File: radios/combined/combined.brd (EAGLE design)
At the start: 31.9 x 30.9 mm, 20 parts

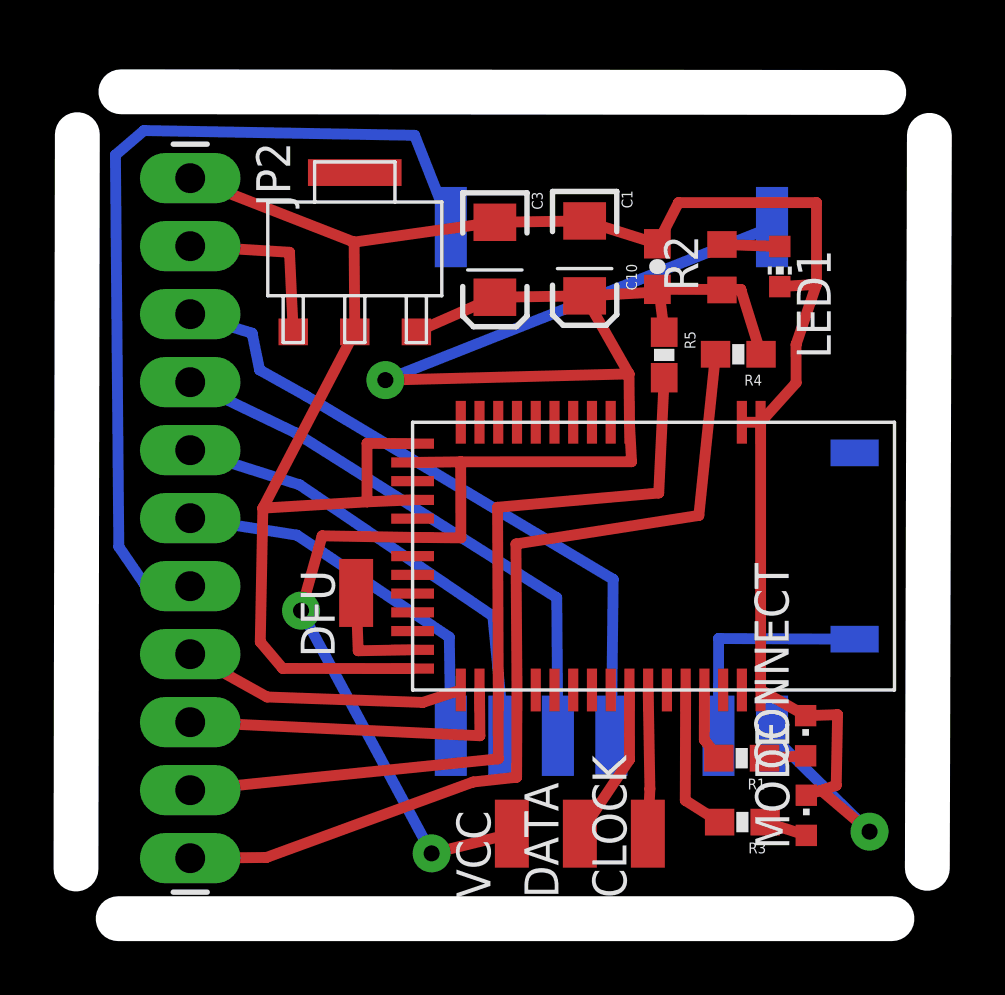
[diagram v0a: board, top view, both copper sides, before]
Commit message: redesigned radios breakout
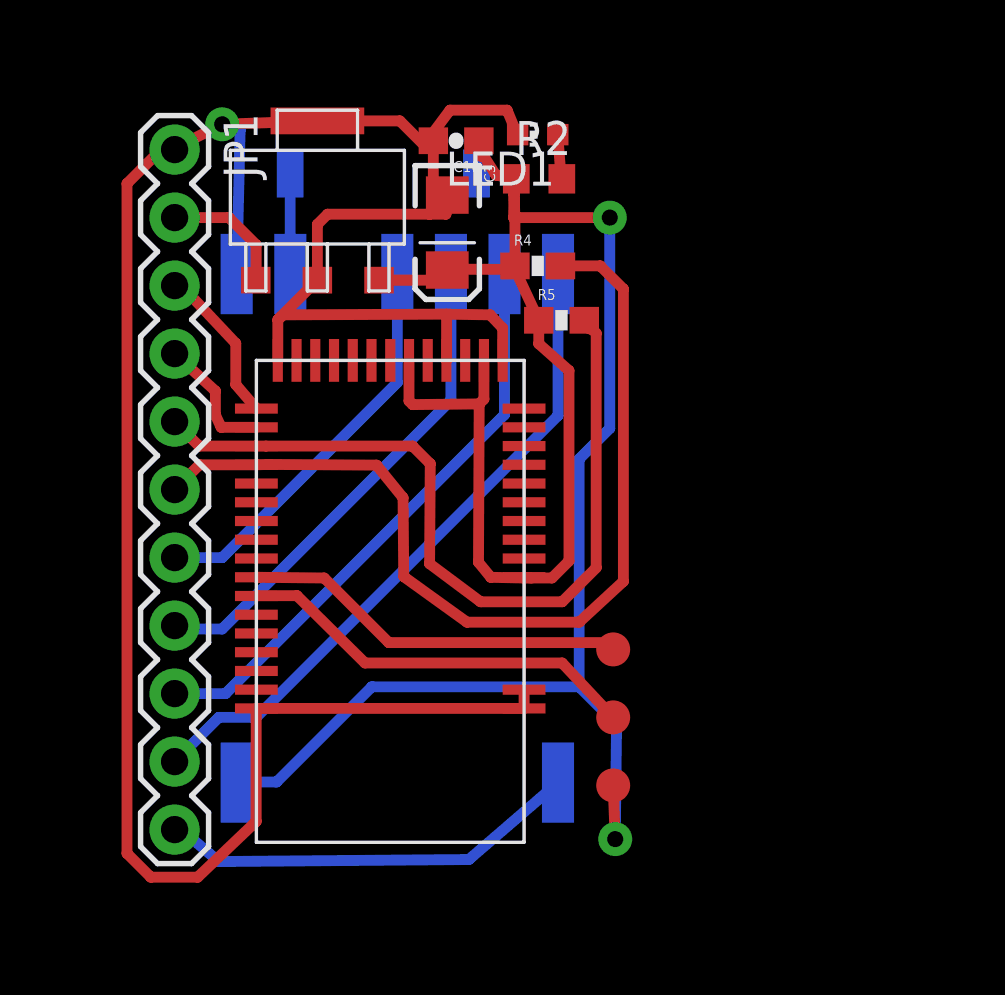
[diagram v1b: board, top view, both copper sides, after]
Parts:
- removed C1: 10uF, SparkFun-Capacitors:EIA3216
- removed CONNECT, MODE: (no value), adafruit:CHIPLED_0603
- removed DFU: (no value), wirepad:SMD1,27-2,54
- removed JP2: M11LONGPADS, SparkFun-Connectors:1X11_LONGPADS
- removed R1, R3: 1k, SparkFun-Resistors:0603-RES
- added JP1: M11PTH, SparkFun-Connectors:1X11
- CLOCK, DATA, VCC: value (none) -> PAD; device wirepad:SMD1,27-2,54 -> ITP_Lab:SMD-ROUND
- U$1: device ITP_Lab:RFM69 -> ITP_Lab:S0C-RFM69
- U$3: value 3.3V-REG-LARGE -> REGULATOR3.3V-UA78M33CDCYR
- moved U$2 22.4 mm to (10.3, 26.9), turned to 180 degrees
- moved LED1 10.3 mm to (16.1, 28.4), turned to 90 degrees
- moved C10 8.87 mm to (13.1, 28.1), turned to 180 degrees
- moved U$4 8.54 mm to (10.5, 12.3), turned to 180 degrees
- moved R4 8.19 mm to (16.1, 23.5), turned to 0 degrees
- moved R2 7.59 mm to (16.2, 26.7), turned to 0 degrees
- moved DATA 7.00 mm to (18.9, 9.14)
- moved U$1 6.25 mm to (11.9, 13.7), turned to 90 degrees
- moved CLOCK 4.53 mm to (18.9, 6.60)
- moved VCC 4.19 mm to (18.9, 4.06)
- moved R5 4.05 mm to (17.0, 21.4), turned to 0 degrees
- moved U$3 2.38 mm to (7.87, 26.0)
- moved C3 2.05 mm to (12.7, 24.7)
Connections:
- removed net N$10: MODE.A, R3.1
- removed net N$13: DFU.1, U$4.P0.07
- removed net N$7: R1.2, U$4.P0.19
- removed net N$8: R3.2, U$4.P0.18
- removed net N$9: CONNECT.A, R1.1
- net BT-CTS: now also JP1.5; no longer JP2.10
- net BT-RTS: now also JP1.3; no longer JP2.8
- net BT-RX: now also JP1.6; no longer JP2.11
- net BT-TX: now also JP1.4; no longer JP2.9
- net GND: now also JP1.1, U$3.4; no longer C1.C, CONNECT.C, JP2.1, MODE.C
- net MISO: now also JP1.8; no longer JP2.4
- net MOSI: now also JP1.9; no longer JP2.5
- net N$11: now also CLOCK.P$1; no longer CLOCK.1
- net N$12: now also DATA.P$1; no longer DATA.1
- net RF-REQ: now also JP1.11; no longer JP2.7
- net RF-SS: now also JP1.10; no longer JP2.6
- net SCK: now also JP1.7; no longer JP2.3
- net VCC: now also VCC.P$1; no longer C1.A, VCC.1
- net VIN: now also JP1.2; no longer JP2.2
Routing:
- net RF-REQ: track 33.2 -> 15.8 mm
- net RF-SS: track 14.6 -> 25.0 mm
- net SCK: track 25.0 -> 15.1 mm
- net N$11: track 5.37 -> 15.2 mm
- net N$12: track 5.93 -> 14.4 mm
- net BT-TX: track 12.5 -> 4.79 mm
- net N$8: track 5.64 -> 0.00 mm
- net N$6: track 8.71 -> 3.76 mm
- net BT-RTS: track 10.6 -> 5.94 mm
- net MOSI: track 17.5 -> 21.9 mm
- net N$13: track 4.19 -> 0.00 mm
- net GND: track 91.7 -> 95.3 mm
- net N$7: track 2.74 -> 0.00 mm
- net VCC: track 81.1 -> 83.6 mm, vias 3 -> 2
- net MISO: track 21.1 -> 18.6 mm
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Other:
- board outline removed
- board text removed: "GND Vin RF-SCK RF-MISO RF-MOSI RF-SS RF-REQ BT-RTS BT-TX BT-CTS BT-RX"

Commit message: about to cut board
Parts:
- removed JP1: M11PTH, SparkFun-Connectors:1X11
- added U$5: HEADER-11, ITP_Lab:HEADER-11
- moved DATA 4.33 mm to (19.2, 4.83)
- moved CLOCK 4.33 mm to (19.2, 2.29)
- moved VCC 3.31 mm to (19.2, 7.37)
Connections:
- net BT-CTS: now also U$5.5; no longer JP1.5
- net BT-RTS: now also U$5.3; no longer JP1.3
- net BT-RX: now also U$5.6; no longer JP1.6
- net BT-TX: now also U$5.4; no longer JP1.4
- net GND: now also U$5.1; no longer JP1.1
- net MISO: now also U$5.8; no longer JP1.8
- net MOSI: now also U$5.9; no longer JP1.9
- net RF-REQ: now also U$5.11; no longer JP1.11
- net RF-SS: now also U$5.10; no longer JP1.10
- net SCK: now also U$5.7; no longer JP1.7
- net VIN: now also U$5.2; no longer JP1.2
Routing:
- net VCC: track 83.6 -> 79.2 mm
- net N$11: track 15.2 -> 19.6 mm
- net N$12: track 14.4 -> 17.9 mm
- added copper zone on layer 1, net GND
- added copper zone on layer 16, net GND
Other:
- board outline added: 21.5 x 31.4 mm
